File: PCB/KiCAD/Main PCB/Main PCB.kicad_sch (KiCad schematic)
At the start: 46 parts, among them J1 Conn_01x04, J11 Conn_01x04_MountingPin, J12 Conn_01x04_MountingPin, J2 Conn_01x04, J3 Conn_01x04, J4 Conn_01x04, J5 Conn_01x02, J6 Conn_01x02, Q1 BSS138, Q2 BSS138, U1 Teensy4.1, U2 Teensy4.0

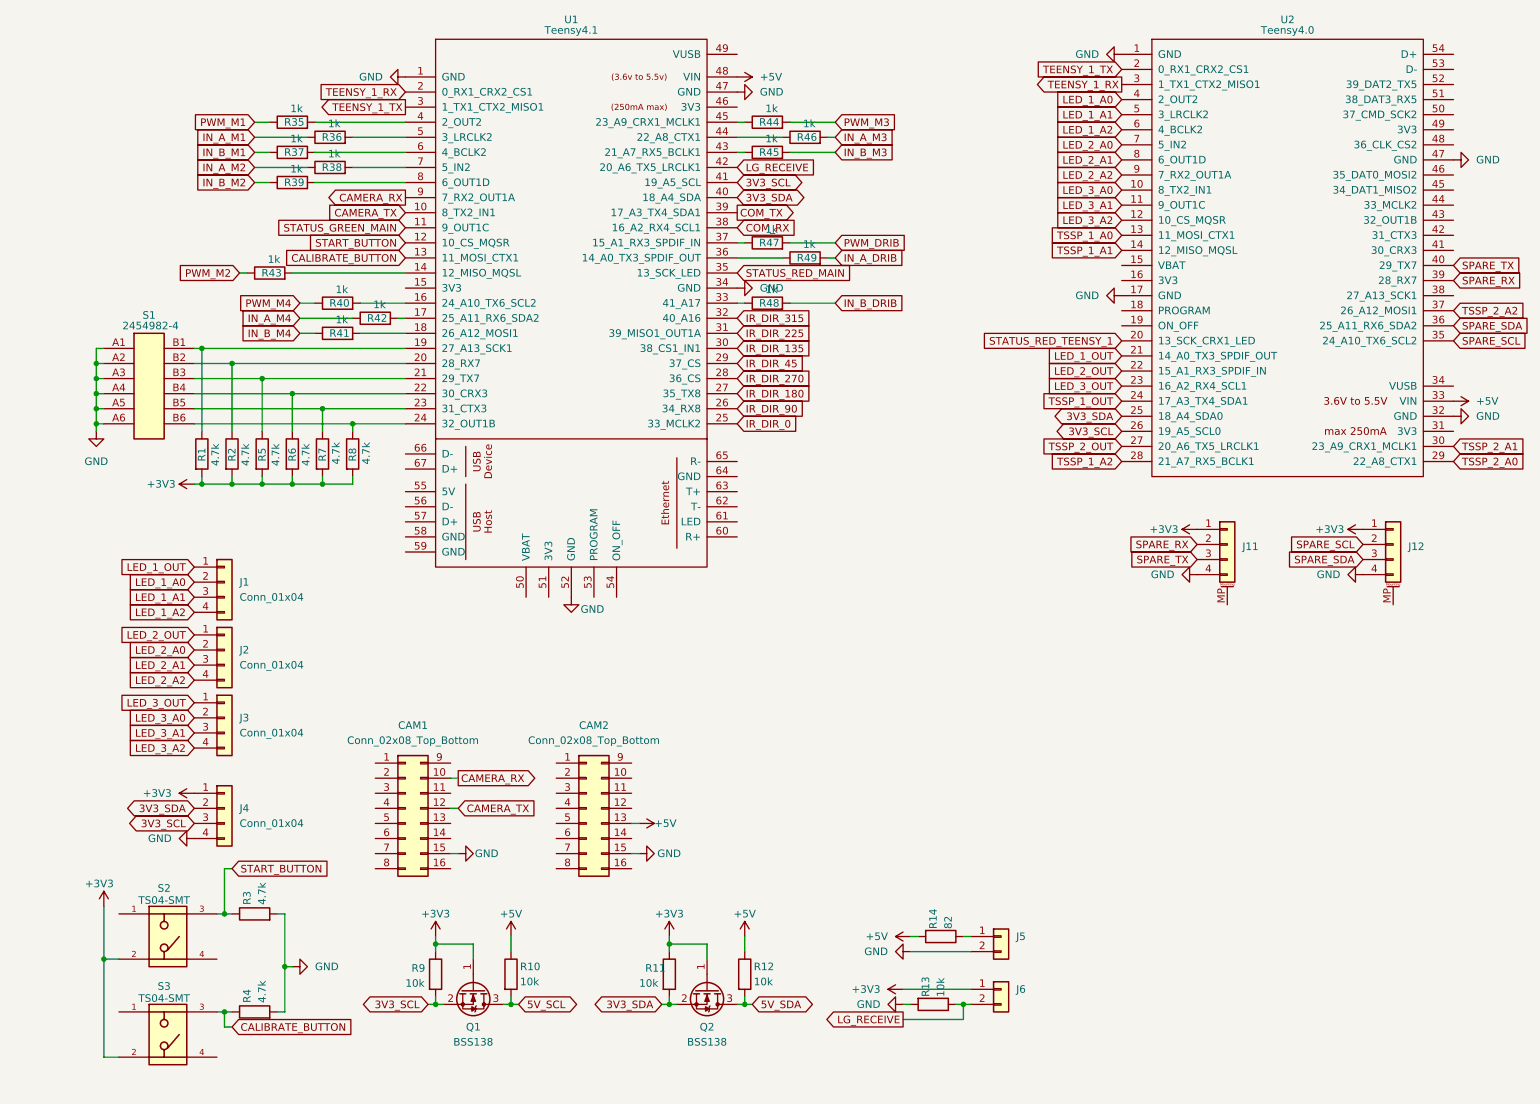
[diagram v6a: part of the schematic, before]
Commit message: Added a BNO055 and traced PCB (incomplete, no DRC pass)
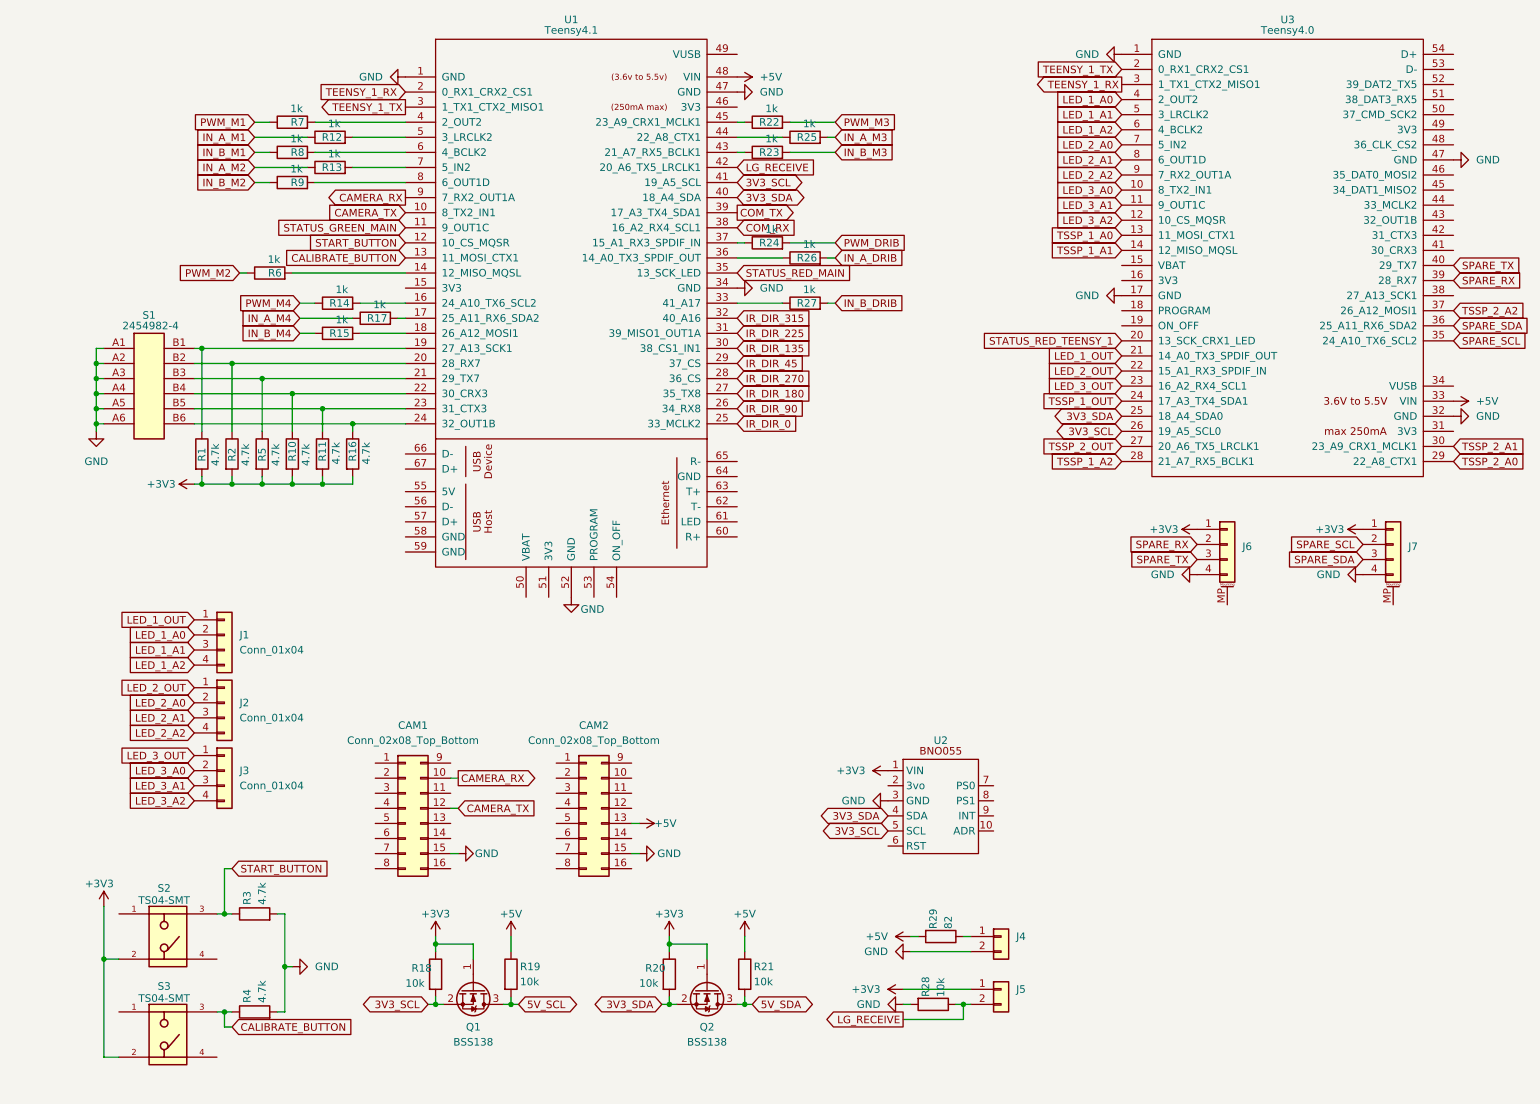
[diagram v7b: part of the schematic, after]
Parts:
- removed J4: Conn_01x04, Connector_JST:JST_PH_B4B-PH-K_1x04_P2.00mm_Vertical, symbol Connector_Generic:Conn_01x04
- added U2: ~, Adafruit:BNO055, symbol Adafruit:BNO055
- renumbered J5 to J4, J6 to J5, J11 to J6, J12 to J7, R6 to R10, R7 to R11, R36 to R12, R38 to R13, R40 to R14, R41 to R15, R8 to R16, R42 to R17, R9 to R18, R10 to R19, R11 to R20, R12 to R21, R44 to R22, R45 to R23, R47 to R24, R46 to R25, R49 to R26, R48 to R27, R13 to R28, R14 to R29, R43 to R6, R35 to R7, R37 to R8, R39 to R9, U2 to U3
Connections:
- net +3V3: now also U2.1 (VIN)
- net 3V3_SCL: now also U2.5 (SCL)
- net 3V3_SDA: now also U2.4 (SDA)
- net GND: now also U2.3 (GND)
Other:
- moved on the sheet: J1, J2, J3, R27

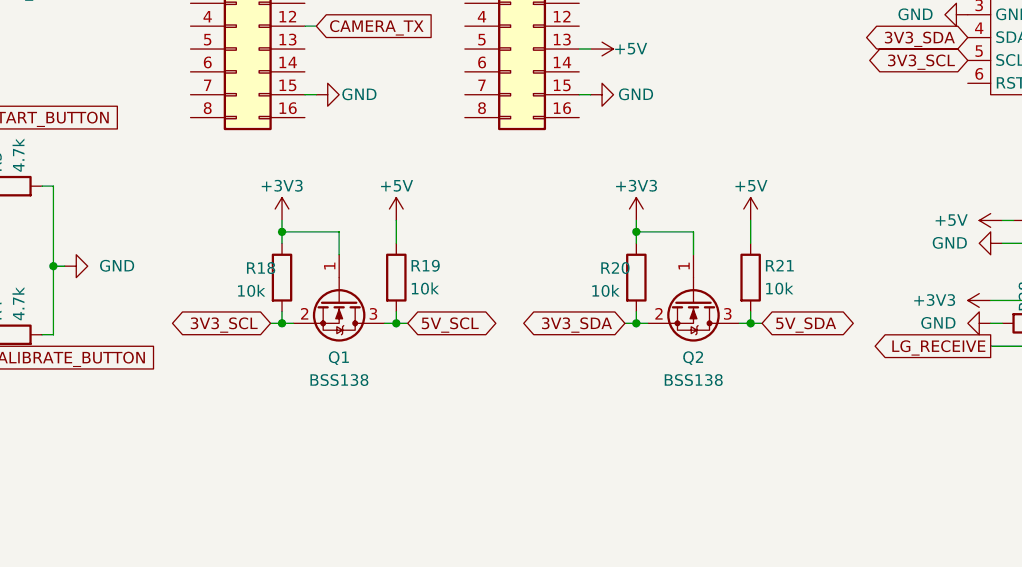
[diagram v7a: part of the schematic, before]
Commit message: Redone main PCB traces and started lower PCB
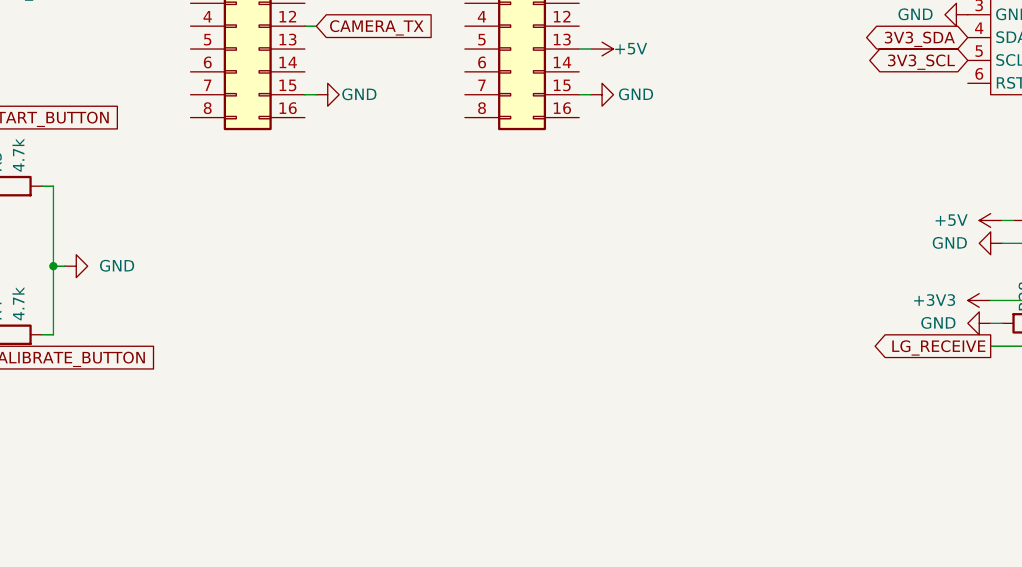
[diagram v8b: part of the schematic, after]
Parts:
- removed Q1, Q2: BSS138, Package_TO_SOT_SMD:SOT-23, symbol Transistor_FET:BSS138
- removed R18, R19, R20, R21: 10k, Resistor_SMD:R_0805_2012Metric_Pad1.20x1.40mm_HandSolder, symbol Device:R
